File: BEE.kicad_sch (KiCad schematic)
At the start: 79 parts, among them J1 RPI1_header, J10 Conn_01x02, J11 Conn_01x02, J12 Conn_01x02, J13 Conn_01x06, J14 Conn_01x03, J15 Conn_02x10_Odd_Even, J16 Conn_01x08, J17 Conn_01x05, J18 Conn_01x03, J19 Conn_01x03, J2 Conn_02x05_Odd_Even, J20 Conn_01x10, J21 Conn_01x03, J3 Conn_01x03, J4 Conn_01x06, J5 Conn_02x10_Odd_Even, J6 Conn_01x06, J7 Conn_02x10_Odd_Even, J8 Conn_01x08, J9 Conn_01x02, SW1 SW_Push, SW2 SW_Push, SW3 SW_Push, U1 MCP3008, U2 MCP4911, U3 Dip_10xsp3t, U4 Dip_10xsp3t, U5 74AHC595, U6 Display_7Segments

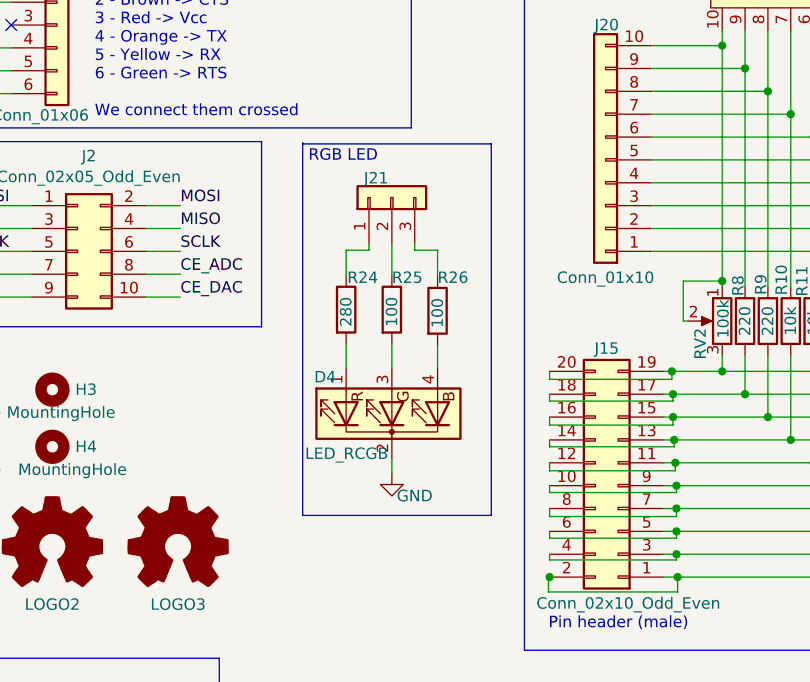
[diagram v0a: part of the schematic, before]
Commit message: changed RGB led by a bigger 5050 one
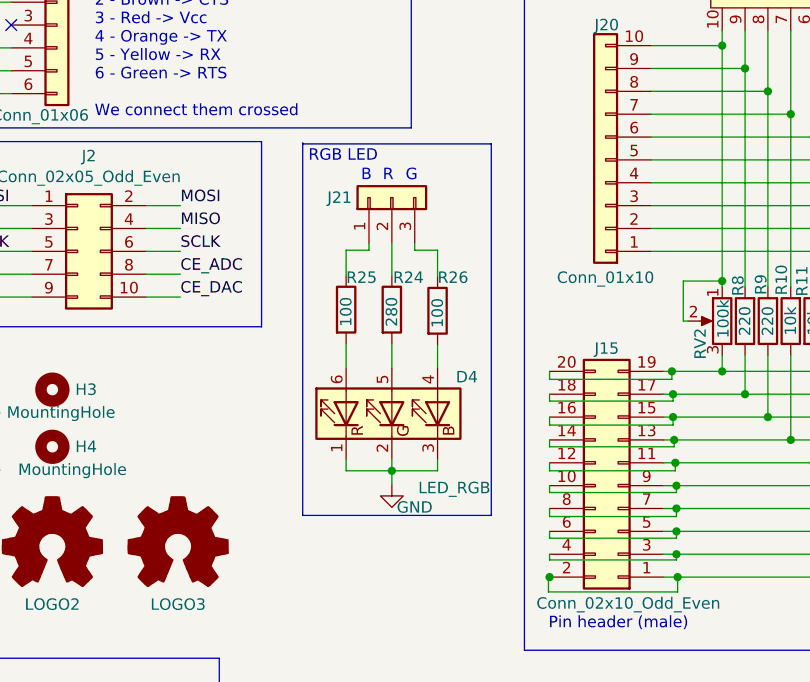
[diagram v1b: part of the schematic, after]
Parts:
- removed D4: LED_RCGB, BEElib:LED_RCGB, symbol BEE:LED_RCGB
- added D4: LED_RGB, LED_SMD:LED_RGB_5050-6, symbol Device:LED_RGB
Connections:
- net GND: now also D4.1 (RK), D4.2 (GK), D4.3 (BK)
- net at R24.2: now also D4.5 (GA)
- net at R25.2: now also D4.6 (RA)
- net at R26.2: now also D4.4 (BA)
- net at R24.1: now also J21.2 (Pin_2); no longer J21.1 (Pin_1)
- net at R25.1: now also J21.1 (Pin_1); no longer J21.2 (Pin_2)
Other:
- note added: "B"
- note added: "G"
- note added: "R"
- moved on the sheet: R24, R25

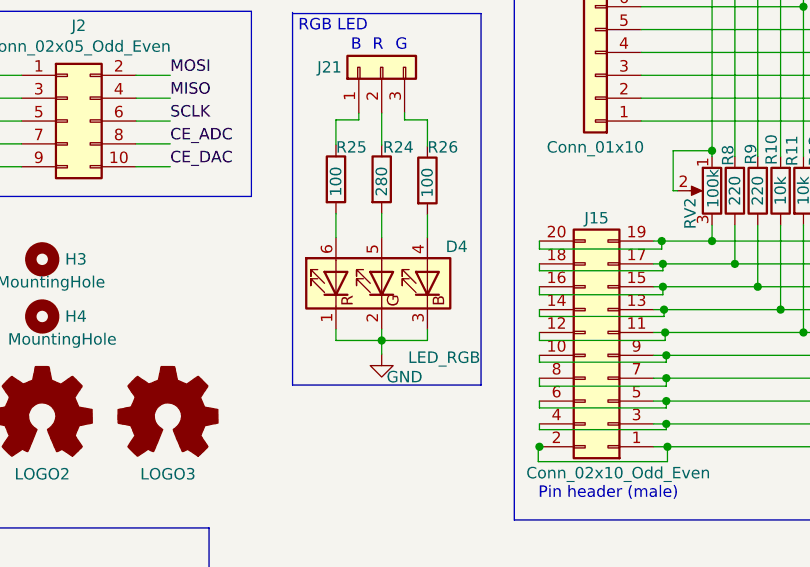
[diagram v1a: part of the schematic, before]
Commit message: D4 pin numbering adjusted on schematic and footprint, according to datasheet
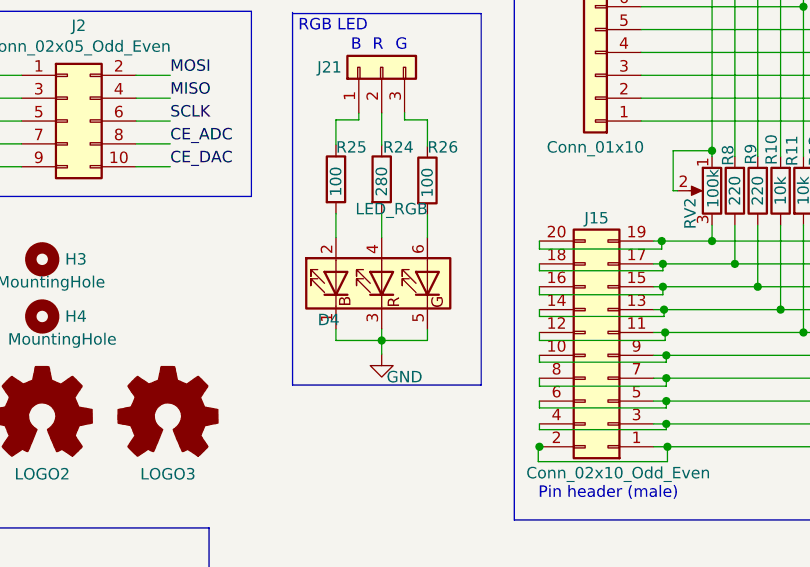
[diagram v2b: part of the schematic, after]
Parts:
- D4: footprint LED_SMD:LED_RGB_5050-6 -> BEElib:LED_RGB_5050-6
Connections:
- net GND: now also D4.5 (BK); no longer D4.2 (GK)
- net at R24.2: now also D4.4 (GA); no longer D4.5 (GA)
- net at R25.2: now also D4.2 (RA); no longer D4.6 (RA)
- net at R26.2: now also D4.6 (BA); no longer D4.4 (BA)
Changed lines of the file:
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@@
   (symbol (lib_id "Device:LED_RGB") (at 172.593 132.461 90) (unit 1)
     (in_bom yes) (on_board yes)
-    (property "Reference" "D4" (id 0) (at 179.705 128.397 90)
+    (property "Reference" "D4" (id 0) (at 165.481 136.525 90)
       (effects (font (size 1.27 1.27)) (justify right))
     )
-    (property "Value" "LED_RGB" (id 1) (at 175.514 140.716 90)
+    (property "Value" "LED_RGB" (id 1) (at 169.672 124.206 90)
       (effects (font (size 1.27 1.27)) (justify right))
     )
-    (property "Footprint" "LED_SMD:LED_RGB_5050-6" (id 2) (at 173.863 132.461 0)
-      (effects (font (size 1.27 1.27)) hide)
-    )
-    (property "Datasheet" "https://www.mouser.es/datasheet/2/445/150505M173300-1715297.pdf" (id 3) (at 173.863 132.461 0)
+    (property "Footprint" "BEElib:LED_RGB_5050-6" (id 2) (at 171.323 132.461 0)
+      (effects (font (size 1.27 1.27)) hide)
+    )
+    (property "Datasheet" "https://www.mouser.es/datasheet/2/445/150505M173300-1715297.pdf" (id 3) (at 171.323 132.461 0)
       (effects (font (size 1.27 1.27)) hide)
     )
@@
     )
     (pin "1")
-    (pin "2")
     (pin "3")
-    (pin "4")
     (pin "5")
     (pin "6")
+    (pin "4")
+    (pin "2")
   )
   (symbol (lib_id "power:+3.3V") (at 17.78 44.45 0) (unit 1)
@@
     )
     (path "/2cf158c2-508a-432c-ba85-07cefc99e466"
-      (reference "D4") (unit 1) (value "LED_RGB") (footprint "LED_SMD:LED_RGB_5050-6")
+      (reference "D4") (unit 1) (value "LED_RGB") (footprint "BEElib:LED_RGB_5050-6")
     )
     (path "/00000000-0000-0000-0000-00005e028b4f"

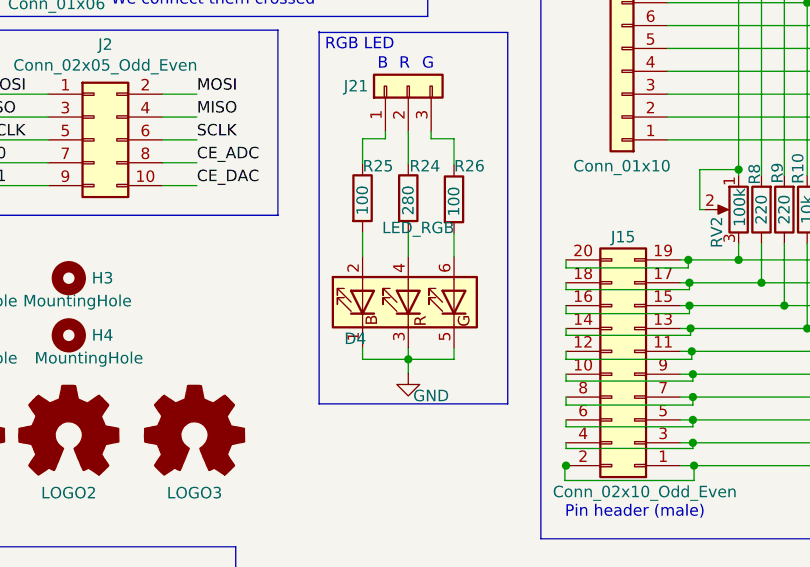
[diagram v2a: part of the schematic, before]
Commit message: renombrado de Manufacturer PN a MPN. borrado ficheros versión anterior
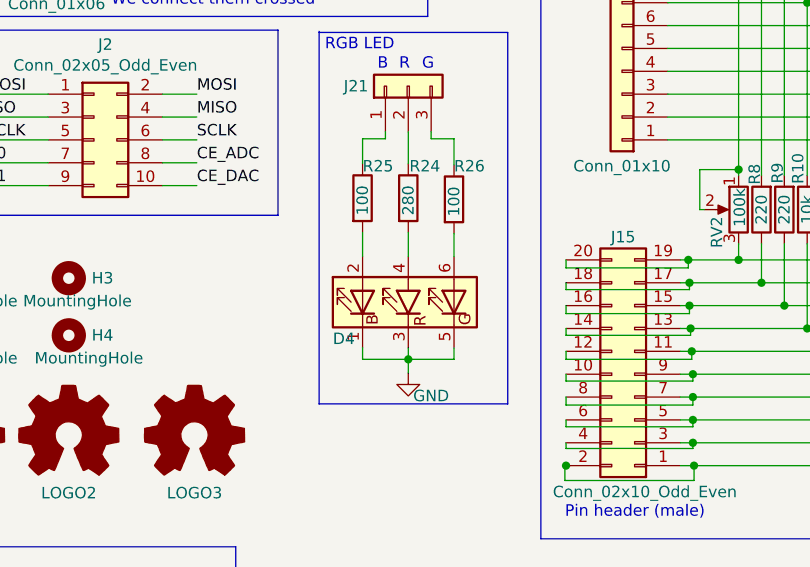
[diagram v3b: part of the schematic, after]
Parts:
- BZ1: MPN (none) -> PS1720P02; Manufacturer PN PS1720P02 -> (none)
- C1, C6: MPN (none) -> C0805C105K4RACTU; Manufacturer PN C0805C105K4RACTU -> (none)
- C2, C4, C5: MPN (none) -> C0805C104K3RACTU; Manufacturer PN C0805C104K3RACTU -> (none)
- C3: MPN (none) -> TAJP106K006RNJ; Manufacturer PN TAJP106K006RNJ -> (none)
- D1, D2, D3: MPN (none) -> 150080RS75000; Manufacturer PN 150080RS75000 -> (none)
- D4: value LED_RGB -> (none); symbol Device:LED_RGB -> BEE:LED_RGB; MPN (none) -> 150505M173300; Manufacturer PN 150505M173300 -> (none)
- J1: MPN (none) -> 7-146254-0; Manufacturer PN 7-146254-0 -> (none)
- J10, J11, J12, J9: MPN (none) -> 68001-402HLF; Manufacturer PN 68001-402HLF -> (none)
- J13, J4, J6: MPN (none) -> 22-28-4060; Manufacturer PN 22-28-4060 -> (none)
- J14, J18, J19, J21, J3: MPN (none) -> 68001-403HLF; Manufacturer PN 68001-403HLF -> (none)
- J15, J5: MPN (none) -> 77313-418-20LF; Manufacturer PN 77313-418-20LF -> (none)
- J16, J8: MPN (none) -> 68000-408HLF; Manufacturer PN 68000-408HLF -> (none)
- J17: MPN (none) -> 10129378-905001BLF; Manufacturer PN 10129378-905001BLF -> (none)
- J2: MPN (none) -> 67997-210HLF; Manufacturer PN 67997-210HLF -> (none)
- J20: MPN (none) -> 10129378-910001BLF; Manufacturer PN 10129378-910001BLF -> (none)
- J7: MPN (none) -> 61301021821; Manufacturer PN 61301021821 -> (none)
- R1, R16, R17, R18, R19, R2, R20, R21, R22, R23, R3, R8, R9: MPN (none) -> CRCW0805220RFKEAC; Manufacturer PN CRCW0805220RFKEAC -> (none)
- R10, R11, R4, R5, R6: MPN (none) -> CRCW080510K0FKEAC; Manufacturer PN CRCW080510K0FKEAC -> (none)
- R12, R13: MPN (none) -> CRCW080515K0FKEAC; Manufacturer PN CRCW080515K0FKEAC -> (none)
- R14, R15: MPN (none) -> CRCW080547K0FKEAC; Manufacturer PN CRCW080547K0FKEAC -> (none)
- R24: MPN (none) -> RT0805FRE07280RL; Manufacturer PN RT0805FRE07280RL -> (none)
- R25, R26: MPN (none) -> RT0805FRE07100RL; Manufacturer PN RT0805FRE07100RL -> (none)
- R7: MPN (none) -> AC0805FR-070RL; Manufacturer PN AC0805FR-070RL -> (none)
- RV1, RV2: MPN (none) -> PVG5A104C03R00; Manufacturer PN PVG5A104C03R00 -> (none)
- SW1, SW2, SW3: MPN (none) -> LL3301NF065QG; Manufacturer PN LL3301NF065QG -> (none)
- U1: MPN (none) -> MCP3008T-I/SL; Manufacturer PN MCP3008T-I/SL -> (none)
- U2: MPN (none) -> CP3008T-I/SL; Manufacturer PN CP3008T-I/SL -> (none)
- U3, U4: MPN (none) -> TDS10SGRNTU04; Manufacturer PN TDS10SGRNTU04 -> (none)
- U5: Distributor (none) -> Mouser; Distributor PN (none) -> 621-74AHC595S16-13; Distributor link (none) -> https://www.mouser.es/ProductDetail/Diodes-Incorporated/74A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; MPN (none) -> 74AHC595S16-13; Manufacturer (none) -> Diodes Incorporated
- U6: MPN (none) -> TDSR1360-IK; Manufacturer PN TDSR1360-IK -> (none)

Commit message: changes for fabrication
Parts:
- BZ1: value /re -> (none); footprint BEElib:Buzzer -> (none)
- C1, C6: value 1uF -> (none); footprint Capacitor_SMD:C_0805_2012Metric_Pad1.18x1.45mm_HandSolder -> (none)
- C2, C4, C5: value 0.1uF -> (none); footprint Capacitor_SMD:C_0805_2012Metric_Pad1.18x1.45mm_HandSolder -> (none)
- C3: value 10uF -> (none); footprint Capacitor_Tantalum_SMD:CP_EIA-2012-15_AVX-P_Pad1.30x1.05mm_HandSolder -> (none)
- D1, D2, D3: value LED -> (none); footprint LED_SMD:LED_0805_2012Metric_Pad1.15x1.40mm_HandSolder -> (none)
- D4: footprint BEElib:LED_RGB_5050-6 -> (none)
- FID1, FID2, FID3: value Fiducial -> (none); footprint Fiducial:Fiducial_0.5mm_Dia_1mm_Outer -> (none)
- H1, H2, H3, H4: value MountingHole -> (none); footprint MountingHole:MountingHole_2.7mm_M2.5 -> (none)
- J1: value RPI1_header -> (none); footprint Connector_PinHeader_2.54mm:PinHeader_2x20_P2.54mm_Vertical -> (none); Distributor PN 571-7-146254-0 -> 649-77313-118-40LF; Distributor link https://www.mouser.es/ProductDetail/TE-Connectivity-AMP/7-1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 -> https://www.mouser.es/ProductDetail/Amphenol-FCI/77313-118-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; MPN 7-146254-0 -> 77313-118-40LF; Manufacturer TE Connectivity / AMP -> Amphenol FCI
- J10, J11, J12, J9: value Conn_01x02 -> (none); footprint Connector_PinHeader_2.54mm:PinHeader_1x02_P2.54mm_Vertical -> (none); Distributor PN 649-68001-402HLF -> 649-1012937890201BLF; Distributor link https://www.mouser.es/ProductDetail/Amphenol-FCI/68001-402H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 -> https://www.mouser.es/ProductDetail/Amphenol-FCI/10129378-9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; MPN 68001-402HLF -> 10129378-902001BLF
- J13, J4, J6: value Conn_01x06 -> (none); footprint Connector_PinHeader_2.54mm:PinHeader_1x06_P2.54mm_Vertical -> (none); Distributor PN 538-22-28-4060 -> 523-G800W302018EU; Distributor link https://www.mouser.es/ProductDetail/Molex/22-28-4060?qs=sGA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 -> https://www.mouser.es/ProductDetail/Amphenol-Commercial-Pro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; MPN 22-28-4060 -> G800W302018EU; Manufacturer Molex -> Amphenol Commercial Products
- J14, J18, J19, J21, J3: value Conn_01x03 -> (none); footprint Connector_PinHeader_2.54mm:PinHeader_1x03_P2.54mm_Vertical -> (none)
- J15, J5: value Conn_02x10_Odd_Even -> (none); footprint Connector_PinHeader_2.54mm:PinHeader_2x10_P2.54mm_Vertical -> (none)
- J16, J8: value Conn_01x08 -> (none); footprint Connector_PinHeader_2.54mm:PinHeader_1x08_P2.54mm_Vertical -> (none)
- J17: value Conn_01x05 -> (none); footprint Connector_PinHeader_2.54mm:PinHeader_1x05_P2.54mm_Vertical -> (none)
- J2: value Conn_02x05_Odd_Even -> (none); footprint Connector_PinHeader_2.54mm:PinHeader_2x05_P2.54mm_Vertical -> (none)
- J20: value Conn_01x10 -> (none); footprint Connector_PinHeader_2.54mm:PinHeader_1x10_P2.54mm_Vertical -> (none)
- J7: value Conn_02x10_Odd_Even -> (none); footprint Connector_PinSocket_2.54mm:PinSocket_2x10_P2.54mm_Vertical -> (none)
- LOGO1: value Logo_Open_Hardware_Small -> (none); footprint Symbol:OSHW-Logo2_7.3x6mm_SilkScreen -> (none)
- LOGO2: value Logo_Open_Hardware_Small -> (none); footprint BEElib:bee_logo2 -> (none)
- LOGO3: value Logo_Open_Hardware_Small -> (none); footprint BEElib:UCMLogo_169_169 -> (none)
- R1, R16, R17, R18, R19, R2, R20, R21, R22, R23, R3, R8, R9: value 220 -> (none); footprint Resistor_SMD:R_0805_2012Metric_Pad1.20x1.40mm_HandSolder -> (none)
- R10, R11, R4, R5, R6: value 10k -> (none); footprint Resistor_SMD:R_0805_2012Metric_Pad1.20x1.40mm_HandSolder -> (none)
- R12, R13: value 15k -> (none); footprint Resistor_SMD:R_0805_2012Metric_Pad1.20x1.40mm_HandSolder -> (none)
- R14, R15: value 47k -> (none); footprint Resistor_SMD:R_0805_2012Metric_Pad1.20x1.40mm_HandSolder -> (none)
- R24: value 280 -> (none); footprint Resistor_SMD:R_0805_2012Metric_Pad1.20x1.40mm_HandSolder -> (none)
- R25, R26: value 100 -> (none); footprint Resistor_SMD:R_0805_2012Metric_Pad1.20x1.40mm_HandSolder -> (none)
- R7: value 0 -> (none); footprint Resistor_SMD:R_0805_2012Metric_Pad1.20x1.40mm_HandSolder -> (none)
- RV1, RV2: value 100k -> (none); footprint BEElib:POT_PVG5A -> (none)
- SW1, SW2, SW3: value SW_Push -> (none); footprint BEElib:PushButton -> (none)
- U1: value MCP3008 -> (none); footprint Package_SO:SOIC-16_3.9x9.9mm_P1.27mm -> (none)
- U2: value MCP4911 -> (none); footprint Package_SO:SOIC-8_3.9x4.9mm_P1.27mm -> (none); MPN CP3008T-I/SL -> MCP4911-E/MS
- U3, U4: value Dip_10xsp3t -> (none); footprint BEElib:dip_10xsp3t -> (none); Alternative Distributor Link (none) -> https://www.onlinecomponents.com/en/te-connectivity-pb-bran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
- U5: value 74AHC595 -> (none); footprint Package_SO:SOIC-16_3.9x9.9mm_P1.27mm -> (none)
- U6: value Display_7Segments -> (none); footprint BEElib:7segments -> (none)
